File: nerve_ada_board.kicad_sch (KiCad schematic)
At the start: 21 parts, among them SW1 SW_Push, SW2 SW_SPDT, U1 stm32f446ret, Y1 8MHz 16pF

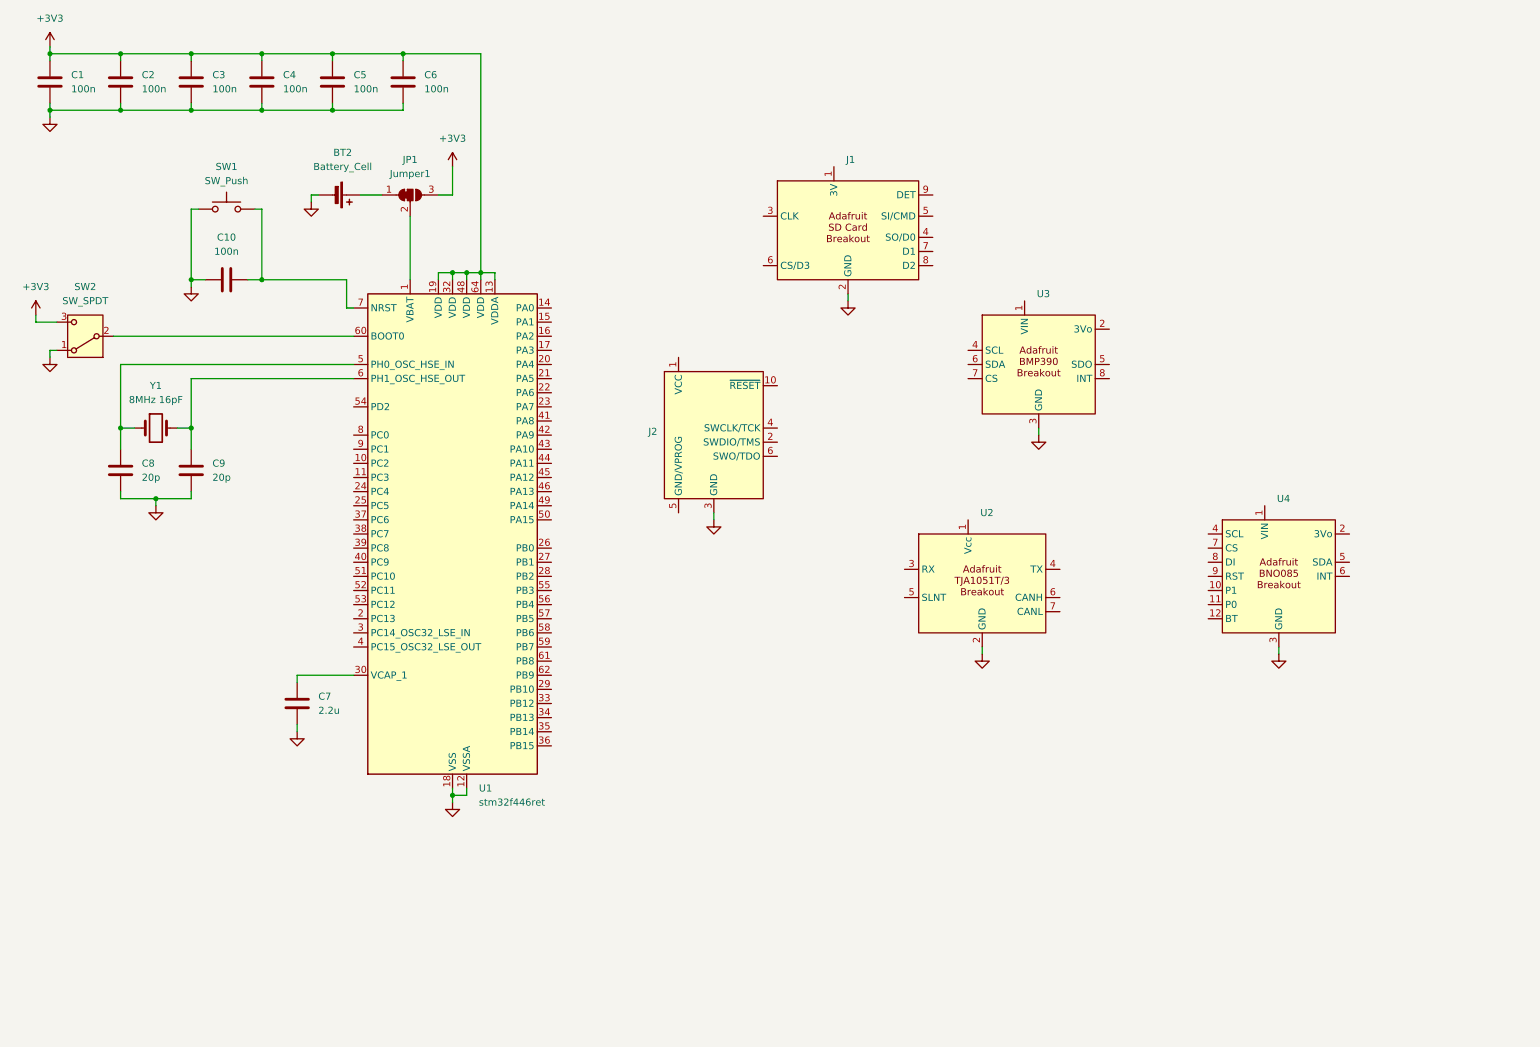
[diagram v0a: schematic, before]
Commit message: Add WIP basics, power and sensors
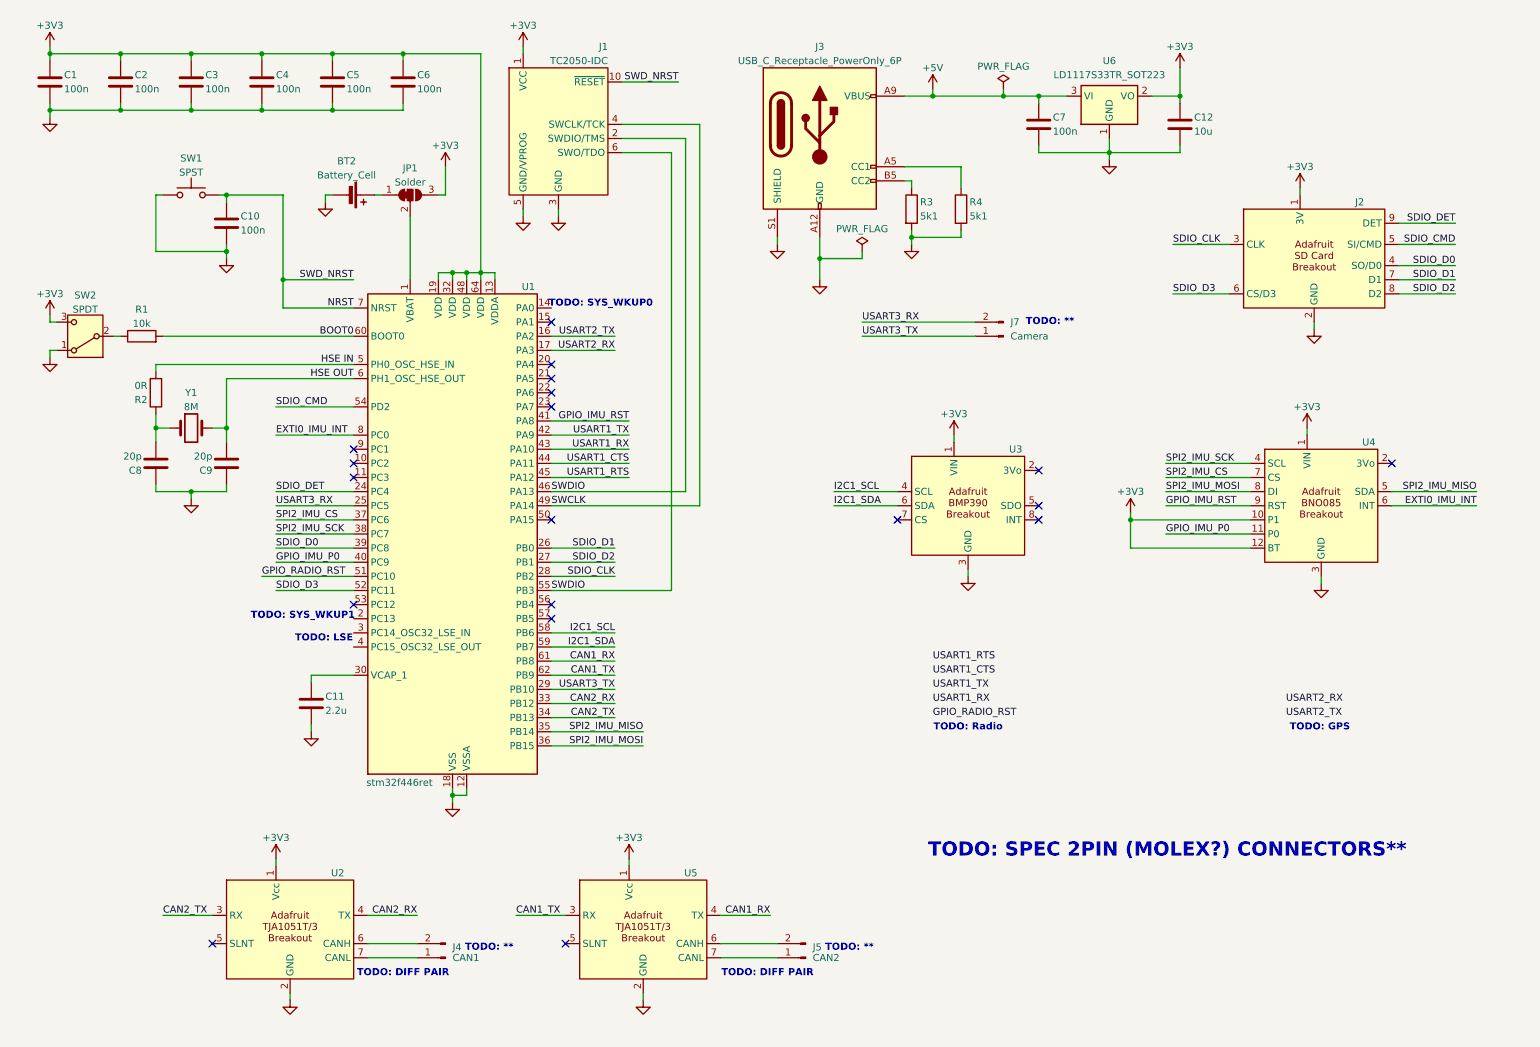
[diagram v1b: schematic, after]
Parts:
- removed J1: ~, adafruit:adafruit_4682_sdio_card, symbol adafruit:adafruit_4682_sdio_card
- added C11: 2.2u, symbol Device:C
- added C12: 10u, symbol Device:C
- added J2: ~, adafruit:adafruit_4682_sdio_card, symbol adafruit:adafruit_4682_sdio_card
- added J3: USB_C_Receptacle_PowerOnly_6P, symbol Connector:USB_C_Receptacle_PowerOnly_6P
- added J4: CAN1, symbol Connector:Conn_01x02_Pin
- added J5: CAN2, symbol Connector:Conn_01x02_Pin
- added J7: Camera, symbol Connector:Conn_01x02_Pin
- added R1: 10k, symbol Device:R
- added R2: 0R, symbol Device:R
- added R3, R4: 5k1, symbol Device:R
- added U5: ~, adafruit:adafruit_5708_tja1051t-3, symbol adafruit:adafruit_5708_tja1051t-3
- added U6: LD1117S33TR_SOT223, Package_TO_SOT_SMD:SOT-223-3_TabPin2, symbol Regulator_Linear:LD1117S33TR_SOT223
- C7: value 2.2u -> 100n
- J1: renamed from J2; value ~ -> TC2050-IDC
- JP1: value Jumper1 -> Solder
- SW1: value SW_Push -> SPST
- SW2: value SW_SPDT -> SPDT
- Y1: value 8MHz 16pF -> 8M
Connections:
- net +3V3: now also J1.1 (VCC), U2.1 (Vcc), U3.1 (VIN), U4.1 (VIN), U4.10 (P1), U4.12 (BT), C12.1, J2.1 (3V), U5.1 (Vcc), U6.2 (VO)
- net GND: now also C8.1, C9.1, J1.5 (GND/VPROG), C11.2, C12.2, J2.2 (GND), J3.A12 (GND), J3.B12 (GND), J3.S1 (SHIELD), R3.2, R4.2, U5.2 (GND), U6.1 (GND); no longer C8.2, C9.2
- net I2C1_SCL: now reaches U3.4 (SCL)
- net I2C1_SCL: now also U1.58 (PB6)
- net I2C1_SDA: now reaches U3.6 (SDA)
- net I2C1_SDA: now also U1.59 (PB7)
- net NRST: now reaches C10.2, SW1.2, U1.7 (NRST)
- net NRST: now also J1.10 (~{RESET})
- net at SW2.2 (B): now also R1.1; no longer U1.60 (BOOT0)
- net HSE OUT: now reaches U1.6 (PH1_OSC_HSE_OUT), Y1.2
- net HSE OUT: now also C9.2; no longer C9.1
- net CAN2_TX: now reaches U2.3 (RX)
- net CAN2_TX: now also U1.34 (PB13)
- net CAN2_RX: now reaches U2.4 (TX)
- net CAN2_RX: now also U1.33 (PB12)
- net at U2.6 (CANH): now also J4.2 (Pin_2)
- net at U2.7 (CANL): now also J4.1 (Pin_1)
- net USART2_TX: now reaches U1.16 (PA2)
- net USART2_RX: now reaches U1.17 (PA3)
- net SDIO_DET: now reaches U1.24 (PC4)
- net SDIO_DET: now also J2.9 (DET)
- net USART3_RX: now reaches U1.25 (PC5)
- net USART3_RX: now also J7.2 (Pin_2)
- net SDIO_D1: now reaches U1.26 (PB0)
- net SDIO_D1: now also J2.7 (D1)
- net SDIO_D2: now reaches U1.27 (PB1)
- net SDIO_D2: now also J2.8 (D2)
- net SDIO_CLK: now reaches U1.28 (PB2)
- net SDIO_CLK: now also J2.3 (CLK)
- net USART3_TX: now reaches U1.29 (PB10)
- net USART3_TX: now also J7.1 (Pin_1)
- net at U1.30 (VCAP_1): now also C11.1; no longer C7.1
- net SPI2_IMU_MISO: now reaches U1.35 (PB14)
- net SPI2_IMU_MISO: now also U4.5 (SDA)
- net SPI2_IMU_MOSI: now reaches U1.36 (PB15)
- net SPI2_IMU_MOSI: now also U4.8 (DI)
- net SPI2_IMU_CS: now reaches U1.37 (PC6)
- net SPI2_IMU_CS: now also U4.7 (CS)
- net SPI2_IMU_SCK: now reaches U1.38 (PC7)
- net SPI2_IMU_SCK: now also U4.4 (SCL)
- net SDIO_D0: now reaches U1.39 (PC8)
- net SDIO_D0: now also J2.4 (SO/D0)
- net GPIO_IMU_P0: now reaches U1.40 (PC9)
- net GPIO_IMU_P0: now also U4.11 (P0)
- net GPIO_IMU_RST: now reaches U1.41 (PA8)
- net GPIO_IMU_RST: now also U4.9 (RST)
- net USART1_TX: now reaches U1.42 (PA9)
- net USART1_RX: now reaches U1.43 (PA10)
- net USART1_CTS: now reaches U1.44 (PA11)
- net USART1_RTS: now reaches U1.45 (PA12)
- net SWDIO: now reaches U1.46 (PA13)
- net SWDIO: now also J1.2 (SWDIO/TMS), J1.6 (SWO/TDO), U1.55 (PB3)
- net SWCLK: now reaches U1.49 (PA14)
- net SWCLK: now also J1.4 (SWCLK/TCK)
- net GPIO_RADIO_RST: now reaches U1.51 (PC10)
- net SDIO_D3: now reaches U1.52 (PC11)
- net SDIO_D3: now also J2.6 (CS/D3)
- net SDIO_CMD: now reaches U1.54 (PD2)
- net SDIO_CMD: now also J2.5 (SI/CMD)
- net CAN1_RX: now reaches U1.61 (PB8)
- net CAN1_RX: now also U5.4 (TX)
- net CAN1_TX: now reaches U1.62 (PB9)
- net CAN1_TX: now also U5.3 (RX)
- net EXTI0_IMU_INT: now reaches U1.8 (PC0)
- net EXTI0_IMU_INT: now also U4.6 (INT)
- new net: C8.2, R2.1, Y1.1
- new net: J3.B5 (CC2), R3.1
- new net: J5.2 (Pin_2), U5.6 (CANH)
- new net: J5.1 (Pin_1), U5.7 (CANL)
- new net: J3.A5 (CC1), R4.1
- new net +5V: C7.1, J3.A9 (VBUS), J3.B9 (VBUS), U6.3 (VI)
- new net BOOT0: R1.2, U1.60 (BOOT0)
- new net HSE IN: R2.2, U1.5 (PH0_OSC_HSE_IN)
- no-connect marks 0 -> 19
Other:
- note added: "TODO: **"
- note added: "TODO: DIFF PAIR"
- note added: "TODO: GPS"
- note added: "TODO: LSE"
- note added: "TODO: Radio"
- note added: "TODO: SPEC 2PIN (MOLEX?) CONNECTORS**"
- note added: "TODO: SYS_WKUP0"
- note added: "TODO: SYS_WKUP1"
- moved on the sheet: BT2, C10, C8, C9, J1, SW1, U2, U3, U4, Y1

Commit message: Add XBee radio and u-blox GPS
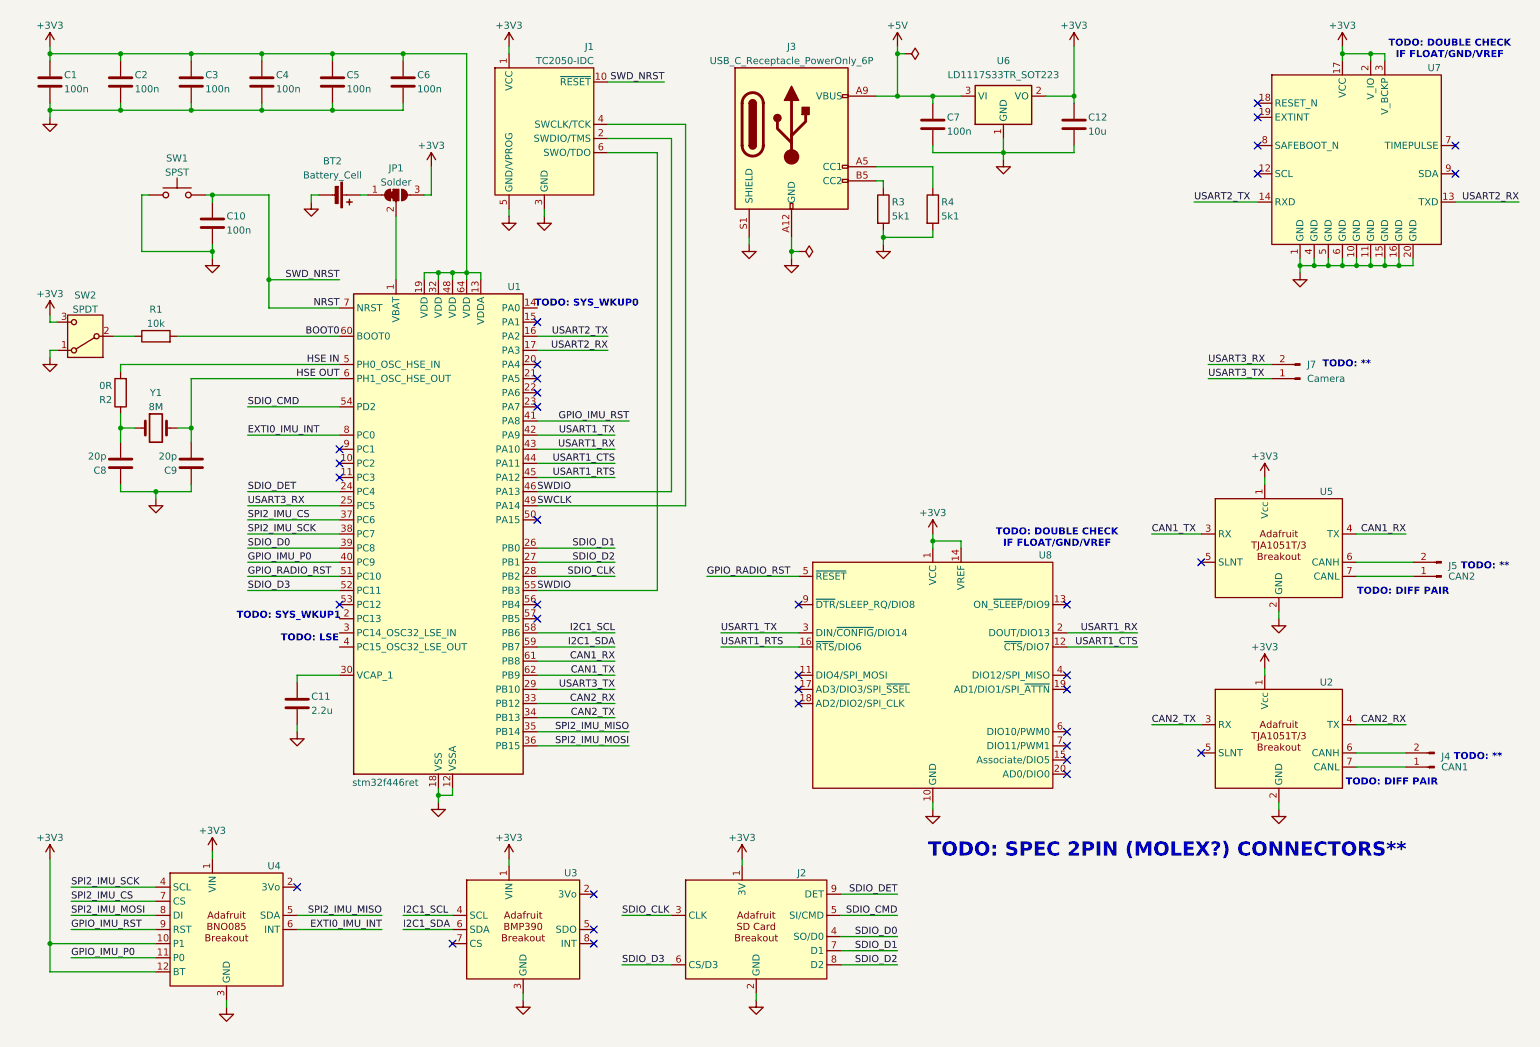
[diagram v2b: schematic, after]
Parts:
- added U7: ~, symbol ublox:ublox_sam-m10q
- added U8: ~, digi_xbee:xbee_pro_900hp, symbol digi_xbee:xbee_pro_900hp
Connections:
- net +3V3: now also U7.17 (VCC), U7.2 (V_IO), U7.3 (V_BCKP), U8.1 (VCC), U8.14 (VREF)
- net GND: now also U7.1 (GND), U7.10 (GND), U7.11 (GND), U7.15 (GND), U7.16 (GND), U7.20 (GND), U7.4 (GND), U7.5 (GND), U7.6 (GND), U8.10 (GND), U8.8 (Reserved)
- net GPIO_RADIO_RST: now also U8.5 (~{RESET})
- net USART1_CTS: now also U8.12 (~{CTS}/DIO7)
- net USART1_RTS: now also U8.16 (~{RTS}/DIO6)
- net USART1_RX: now also U8.2 (DOUT/DIO13)
- net USART1_TX: now also U8.3 (DIN/~{CONFIG}/DIO14)
- net USART2_RX: now also U7.13 (TXD)
- net USART2_TX: now also U7.14 (RXD)
- no-connect marks 19 -> 36
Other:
- note added: "TODO: DOUBLE CHECK IF FLOAT/GND/VREF"
- note removed: "TODO: GPS"
- note removed: "TODO: Radio"
- moved on the sheet: BT2, C10, C11, C12, C7, C8, C9, J1, J2, J3, J4, J5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

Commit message: Add very early full schematic
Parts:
- removed J4: CAN1, symbol Connector:Conn_01x02_Pin
- removed J7: Camera, symbol Connector:Conn_01x02_Pin
- added BT1: CR1220, symbol Device:Battery_Cell
- added C12: 10u, symbol Device:C
- added C14, C15: 1p5, symbol Device:C
- added J3: CAN1, symbol Connector:Conn_01x02_Pin
- added J4: Camera, symbol Connector:Conn_01x04_Pin
- added JP1: Solder, symbol Jumper:SolderJumper_3_Bridged12
- added R4, R7: 10k, symbol Device:R
- added R6, R8, R9: 0R, symbol Device:R
- added SW3, SW4: SPST, symbol Switch:SW_Push
- added Y2: 32.768K, symbol Device:Crystal
- BT2: value Battery_Cell -> CR1220
- C13: renamed from C11; value 2.2u -> 2u2
- J2: renamed from J3; value USB_C_Receptacle_PowerOnly_6P -> USB-C Power Only 6P
- U2: renamed from U7; value ~ -> SAM-M10Q
- U3: renamed from U1; value stm32f446ret -> STM32F446RET
- U5: renamed from U8; value ~ -> XBP9B-DMWT-002
- renumbered C8 to C10, C9 to C11, C12 to C8, C10 to C9, J2 to J6, JP1 to JP2, R3 to R1, R4 to R2, R1 to R3, R2 to R5, U6 to U1, U5 to U4, U2 to U6, U4 to U7, U3 to U8
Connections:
- net +3V3: now also C12.1, JP1.3 (B), R4.1, R7.1; no longer U2.3 (V_BCKP), U5.1 (VCC), U5.14 (VREF), U7.12 (BT)
- net +5V: now also J4.4 (Pin_4)
- net GND: now also C10.2, C11.2, BT1.2 (-), C14.2, C15.2, J4.1 (Pin_1), SW3.2, SW4.1; no longer C10.1, C11.1
- net HSE IN: now also R5.1; no longer R5.2
- net HSE OUT: now also R6.1; no longer C11.2, Y1.2
- net USART3_RX: now also J4.3 (Pin_3)
- net USART3_TX: now also J4.2 (Pin_2)
- net CAN1_HIGH+: now reaches U4.6 (CANH)
- net CAN1_HIGH+: now also J3.2 (Pin_2); no longer J5.2 (Pin_2)
- net CAN1_LOW-: now reaches U4.7 (CANL)
- net CAN1_LOW-: now also J3.1 (Pin_1); no longer J5.1 (Pin_1)
- net GPIO_GPS_RST: now reaches U2.18 (RESET_N)
- net GPIO_GPS_RST: now also U3.15 (PA1)
- net CAN2_LOW-: now reaches U6.7 (CANL)
- net CAN2_LOW-: now also J5.1 (Pin_1)
- net CAN2_HIGH+: now reaches U6.6 (CANH)
- net CAN2_HIGH+: now also J5.2 (Pin_2)
- net at U3.14 (PA0): now also R4.2, SW3.1
- net at U3.2 (PC13): now also R7.2, SW4.2
- net at U3.3 (PC14_OSC32_LSE_IN): now also R8.1
- net at U3.4 (PC15_OSC32_LSE_OUT): now also R9.1
- net SPI2_IMU_CS renamed GPIO_SPI2_CS
- net SPI2_IMU_MISO renamed SPI2_MISO
- net SPI2_IMU_MOSI renamed SPI2_MOSI
- net SPI2_IMU_SCK renamed SPI2_SCK
- new net: C10.1, R5.2, Y1.1
- new net: C11.1, R6.2, Y1.2
- new net: C14.1, R8.2, Y2.1
- new net: C15.1, R9.2, Y2.2
- new net: JP1.2 (C), U2.3 (V_BCKP)
- new net: BT1.1 (+), JP1.1 (A)
- new net: C12.2, U5.1 (VCC), U5.14 (VREF)
- no-connect marks 36 -> 35
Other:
- note added: "Use PR/PD commands to pull-up all unused input pins. Output pins can be left floating."
- note removed: "TODO: **"
- note removed: "TODO: DIFF PAIR"
- note removed: "TODO: DOUBLE CHECK IF FLOAT/GND/VREF"
- note removed: "TODO: LSE"
- note removed: "TODO: SPEC 2PIN (MOLEX?) CONNECTORS**"
- note removed: "TODO: SYS_WKUP0"
- note removed: "TODO: SYS_WKUP1"
- moved on the sheet: C10, C11, C7, C8, J2, R1, R2, R5, U1, U2, Y1
